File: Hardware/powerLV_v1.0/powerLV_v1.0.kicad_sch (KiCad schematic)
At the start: 56 parts, among them J1 Barrel_Jack, J2 12V IN, J3 3v3 Backup, J4 3v3, J5 5V OUT, U1 MP2338GTL-Z, U2 MP2315SGJ-Z, U3 AMS1117-3.3

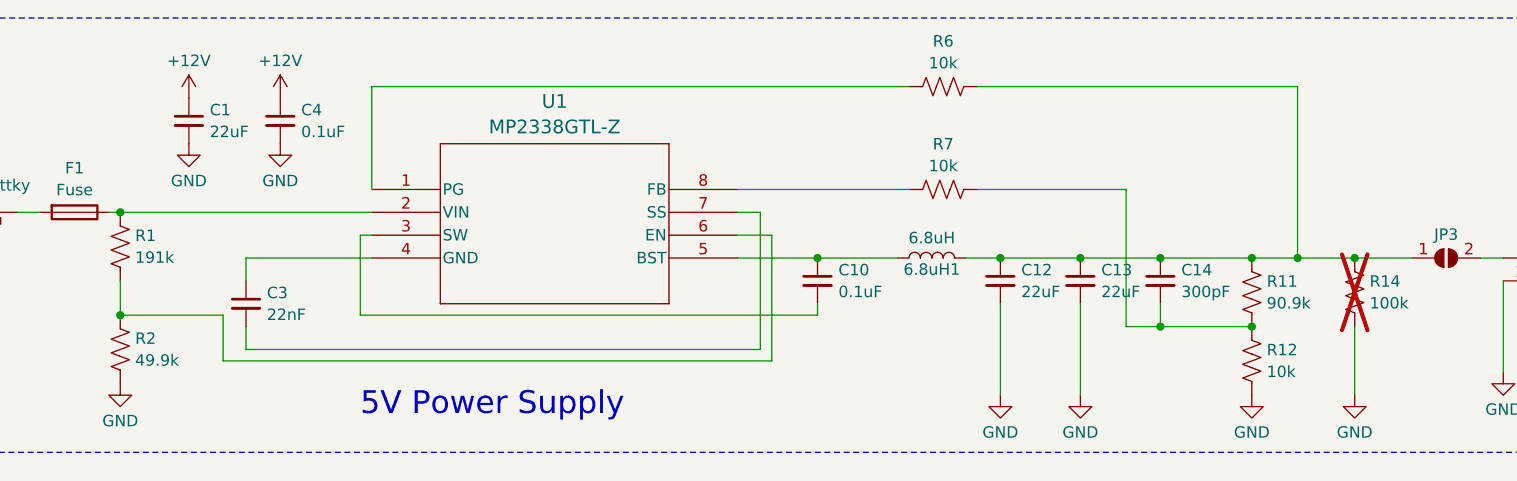
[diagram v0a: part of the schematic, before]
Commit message: instead of an onboard power, I decided to make a separate board for just brain power--essentially a second power board.
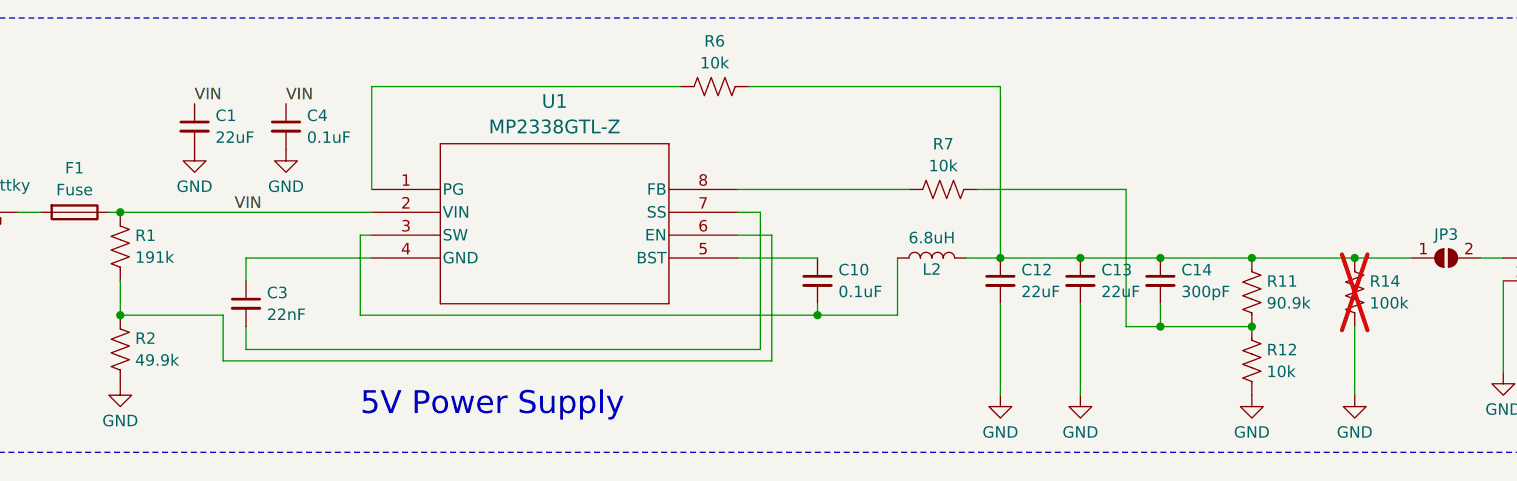
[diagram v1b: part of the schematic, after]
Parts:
- renumbered 6.8uH1 to L2
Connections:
- net +12V: no longer C1.1, C4.1
- net at C10.1, U1.5 (BST): no longer L2.1
- net VIN: now reaches F1.1, R1.1, U1.2 (VIN)
- net VIN: now also C1.1, C4.1
- net at C10.2, U1.3 (SW): now also L2.1
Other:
- moved on the sheet: C1, C4, R6

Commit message: changed LV
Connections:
- net GND: now also C3.1, U1.4 (GND)
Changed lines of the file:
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@@
   (title_block
     (title "Power Board 3v3 and 5V")
-    (date "2025-03-09")
+    (date "2025-04-02")
     (rev "1.0")
     (comment 1 "Designed By: Omkar Kulkarni")
@@
   (junction (at 179.705 43.18) (diameter 0) (color 0 0 0 0)
   )
+  (junction (at 67.945 43.18) (diameter 0) (color 0 0 0 0)
+  )
   (junction (at 151.765 43.18) (diameter 0) (color 0 0 0 0)
   )
@@
     (stroke (width 0) (type default))
   )
+  (wire (pts (xy 63.5 43.18) (xy 67.945 43.18))
+    (stroke (width 0) (type default))
+  )
+  (wire (pts (xy 94.615 181.61) (xy 107.315 181.61))
+    (stroke (width 0) (type default))
+  )
+  (wire (pts (xy 94.615 101.6) (xy 90.805 101.6))
+    (stroke (width 0) (type default))
+  )
+  (wire (pts (xy 42.545 38.1) (xy 45.085 38.1))
+    (stroke (width 0) (type default))
+  )
+  (wire (pts (xy 131.445 48.26) (xy 131.445 49.53))
+    (stroke (width 0) (type default))
+  )
+  (wire (pts (xy 71.755 109.22) (xy 71.755 115.57))
+    (stroke (width 0) (type default))
+  )
+  (wire (pts (xy 187.325 110.49) (xy 194.945 110.49))
+    (stroke (width 0) (type default))
+  )
+  (wire (pts (xy 191.135 50.8) (xy 191.135 58.42))
+    (stroke (width 0) (type default))
+  )
+  (wire (pts (xy 94.615 184.15) (xy 107.315 184.15))
+    (stroke (width 0) (type default))
+  )
+  (wire (pts (xy 31.115 34.29) (xy 31.115 38.1))
+    (stroke (width 0) (type default))
+  )
+  (wire (pts (xy 169.545 50.8) (xy 179.705 50.8))
+    (stroke (width 0) (type default))
+  )
+  (wire (pts (xy 80.645 49.53) (xy 80.645 40.64))
+    (stroke (width 0) (type default))
+  )
+  (wire (pts (xy 37.465 93.98) (xy 37.465 99.06))
+    (stroke (width 0) (type default))
+  )
+  (wire (pts (xy 103.505 144.78) (xy 107.315 144.78))
+    (stroke (width 0) (type default))
+  )
+  (wire (pts (xy 151.765 43.18) (xy 160.655 43.18))
+    (stroke (width 0) (type default))
+  )
+  (wire (pts (xy 125.095 38.1) (xy 122.555 38.1))
+    (stroke (width 0) (type default))
+  )
+  (wire (pts (xy 43.815 144.78) (xy 51.435 144.78))
+    (stroke (width 0) (type default))
+  )
+  (wire (pts (xy 57.785 102.87) (xy 57.785 99.06))
+    (stroke (width 0) (type default))
+  )
+  (wire (pts (xy 135.255 99.06) (xy 139.065 99.06))
+    (stroke (width 0) (type default))
+  )
+  (wire (pts (xy 90.805 101.6) (xy 90.805 110.49))
+    (stroke (width 0) (type default))
+  )
+  (wire (pts (xy 179.705 105.41) (xy 187.325 105.41))
+    (stroke (width 0) (type default))
+  )
+  (wire (pts (xy 94.615 83.82) (xy 86.995 83.82))
+    (stroke (width 0) (type default))
+  )
+  (wire (pts (xy 67.945 50.8) (xy 67.945 53.34))
+    (stroke (width 0) (type default))
+  )
+  (wire (pts (xy 65.405 54.61) (xy 126.365 54.61))
+    (stroke (width 0) (type default))
+  )
+  (wire (pts (xy 57.785 113.03) (xy 139.065 113.03))
+    (stroke (width 0) (type default))
+  )
+  (wire (pts (xy 57.785 99.06) (xy 64.135 99.06))
+    (stroke (width 0) (type default))
+  )
+  (wire (pts (xy 168.275 99.06) (xy 168.275 96.52))
+    (stroke (width 0) (type default))
+  )
+  (wire (pts (xy 79.375 83.82) (xy 86.995 83.82))
+    (stroke (width 0) (type default))
+  )
+  (wire (pts (xy 122.555 35.56) (xy 141.605 35.56))
+    (stroke (width 0) (type default))
+  )
+  (wire (pts (xy 83.82 181.61) (xy 94.615 181.61))
+    (stroke (width 0) (type default))
+  )
+  (wire (pts (xy 125.095 53.34) (xy 125.095 38.1))
+    (stroke (width 0) (type default))
+  )
+  (wire (pts (xy 83.185 144.78) (xy 88.265 144.78))
+    (stroke (width 0) (type default))
+  )
+  (wire (pts (xy 131.445 43.18) (xy 122.555 43.18))
+    (stroke (width 0) (type default))
+  )
+  (wire (pts (xy 177.165 110.49) (xy 187.325 110.49))
+    (stroke (width 0) (type default))
+  )
+  (wire (pts (xy 71.755 144.78) (xy 74.295 144.78))
+    (stroke (width 0) (type default))
+  )
+  (wire (pts (xy 179.705 102.87) (xy 179.705 105.41))
+    (stroke (width 0) (type default))
+  )
+  (wire (pts (xy 155.575 96.52) (xy 168.275 96.52))
+    (stroke (width 0) (type default))
+  )
+  (wire (pts (xy 140.335 49.53) (xy 140.335 43.18))
+    (stroke (width 0) (type default))
+  )
+  (wire (pts (xy 168.275 96.52) (xy 179.705 96.52))
+    (stroke (width 0) (type default))
+  )
+  (wire (pts (xy 37.465 99.06) (xy 40.005 99.06))
+    (stroke (width 0) (type default))
+  )
+  (wire (pts (xy 179.705 97.79) (xy 179.705 96.52))
+    (stroke (width 0) (type default))
+  )
+  (wire (pts (xy 160.655 48.26) (xy 160.655 58.42))
+    (stroke (width 0) (type default))
+  )
+  (wire (pts (xy 94.615 104.14) (xy 94.615 115.57))
+    (stroke (width 0) (type default))
+  )
   (wire (pts (xy 67.945 43.18) (xy 81.915 43.18))
-    (stroke (width 0) (type default))
-  )
-  (wire (pts (xy 94.615 181.61) (xy 107.315 181.61))
-    (stroke (width 0) (type default))
-  )
-  (wire (pts (xy 94.615 101.6) (xy 90.805 101.6))
-    (stroke (width 0) (type default))
-  )
-  (wire (pts (xy 42.545 38.1) (xy 45.085 38.1))
-    (stroke (width 0) (type default))
-  )
-  (wire (pts (xy 131.445 48.26) (xy 131.445 49.53))
-    (stroke (width 0) (type default))
-  )
-  (wire (pts (xy 71.755 109.22) (xy 71.755 115.57))
-    (stroke (width 0) (type default))
-  )
-  (wire (pts (xy 187.325 110.49) (xy 194.945 110.49))
-    (stroke (width 0) (type default))
-  )
-  (wire (pts (xy 191.135 50.8) (xy 191.135 58.42))
-    (stroke (width 0) (type default))
-  )
-  (wire (pts (xy 94.615 184.15) (xy 107.315 184.15))
-    (stroke (width 0) (type default))
-  )
-  (wire (pts (xy 31.115 34.29) (xy 31.115 38.1))
-    (stroke (width 0) (type default))
-  )
-  (wire (pts (xy 169.545 50.8) (xy 179.705 50.8))
-    (stroke (width 0) (type default))
-  )
-  (wire (pts (xy 80.645 49.53) (xy 80.645 40.64))
-    (stroke (width 0) (type default))
-  )
-  (wire (pts (xy 37.465 93.98) (xy 37.465 99.06))
-    (stroke (width 0) (type default))
-  )
-  (wire (pts (xy 103.505 144.78) (xy 107.315 144.78))
-    (stroke (width 0) (type default))
-  )
-  (wire (pts (xy 151.765 43.18) (xy 160.655 43.18))
-    (stroke (width 0) (type default))
-  )
-  (wire (pts (xy 125.095 38.1) (xy 122.555 38.1))
-    (stroke (width 0) (type default))
-  )
-  (wire (pts (xy 43.815 144.78) (xy 51.435 144.78))
-    (stroke (width 0) (type default))
-  )
-  (wire (pts (xy 57.785 102.87) (xy 57.785 99.06))
-    (stroke (width 0) (type default))
-  )
-  (wire (pts (xy 135.255 99.06) (xy 139.065 99.06))
-    (stroke (width 0) (type default))
-  )
-  (wire (pts (xy 90.805 101.6) (xy 90.805 110.49))
-    (stroke (width 0) (type default))
-  )
-  (wire (pts (xy 179.705 105.41) (xy 187.325 105.41))
-    (stroke (width 0) (type default))
-  )
-  (wire (pts (xy 94.615 83.82) (xy 86.995 83.82))
-    (stroke (width 0) (type default))
-  )
-  (wire (pts (xy 67.945 50.8) (xy 67.945 53.34))
-    (stroke (width 0) (type default))
-  )
-  (wire (pts (xy 65.405 54.61) (xy 126.365 54.61))
-    (stroke (width 0) (type default))
-  )
-  (wire (pts (xy 57.785 113.03) (xy 139.065 113.03))
-    (stroke (width 0) (type default))
-  )
-  (wire (pts (xy 57.785 99.06) (xy 64.135 99.06))
-    (stroke (width 0) (type default))
-  )
-  (wire (pts (xy 168.275 99.06) (xy 168.275 96.52))
-    (stroke (width 0) (type default))
-  )
-  (wire (pts (xy 79.375 83.82) (xy 86.995 83.82))
-    (stroke (width 0) (type default))
-  )
-  (wire (pts (xy 122.555 35.56) (xy 141.605 35.56))
-    (stroke (width 0) (type default))
-  )
-  (wire (pts (xy 83.82 181.61) (xy 94.615 181.61))
-    (stroke (width 0) (type default))
-  )
-  (wire (pts (xy 125.095 53.34) (xy 125.095 38.1))
-    (stroke (width 0) (type default))
-  )
-  (wire (pts (xy 83.185 144.78) (xy 88.265 144.78))
-    (stroke (width 0) (type default))
-  )
-  (wire (pts (xy 131.445 43.18) (xy 122.555 43.18))
-    (stroke (width 0) (type default))
-  )
-  (wire (pts (xy 177.165 110.49) (xy 187.325 110.49))
-    (stroke (width 0) (type default))
-  )
-  (wire (pts (xy 71.755 144.78) (xy 74.295 144.78))
-    (stroke (width 0) (type default))
-  )
-  (wire (pts (xy 179.705 102.87) (xy 179.705 105.41))
-    (stroke (width 0) (type default))
-  )
-  (wire (pts (xy 155.575 96.52) (xy 168.275 96.52))
-    (stroke (width 0) (type default))
-  )
-  (wire (pts (xy 140.335 49.53) (xy 140.335 43.18))
-    (stroke (width 0) (type default))
-  )
-  (wire (pts (xy 168.275 96.52) (xy 179.705 96.52))
-    (stroke (width 0) (type default))
-  )
-  (wire (pts (xy 37.465 99.06) (xy 40.005 99.06))
-    (stroke (width 0) (type default))
-  )
-  (wire (pts (xy 179.705 97.79) (xy 179.705 96.52))
-    (stroke (width 0) (type default))
-  )
-  (wire (pts (xy 160.655 48.26) (xy 160.655 58.42))
-    (stroke (width 0) (type default))
-  )
-  (wire (pts (xy 94.615 104.14) (xy 94.615 115.57))
     (stroke (width 0) (type default))
   )
@@
         )
       )
+    )
+  )
+  (symbol (lib_id "power:GND") (at 63.5 43.18 0) (unit 1)
+    (in_bom yes) (on_board yes) (dnp no) (fields_autoplaced)
+    (property "Reference" "#PWR06" (at 63.5 49.53 0)
+      (effects (font (size 1.27 1.27)) hide)
+    )
+    (property "Value" "GND" (at 63.5 47.3131 0)
+      (effects (font (size 1.27 1.27)))
+    )
+    (property "Footprint" "" (at 63.5 43.18 0)
+      (effects (font (size 1.27 1.27)) hide)
+    )
+    (property "Datasheet" "" (at 63.5 43.18 0)
+      (effects (font (size 1.27 1.27)) hide)
+    )
+    (pin "1")
+    (instances
+      (project "powerLV_v1.0"
+        (path "/1e1b062d-fad0-427c-a622-c5b8a80b5268"
+          (reference "#PWR06") (unit 1)
+        )
+      )

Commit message: small fix to LV board
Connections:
- net at R4.1, U2.7 (VCC): now also C7.1
- net at R4.2, R5.1, U2.1 (AAM): no longer C7.1
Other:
- moved on the sheet: C7
